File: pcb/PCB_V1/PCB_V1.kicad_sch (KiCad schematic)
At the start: 13 parts, among them U101 TPS54202DDCR

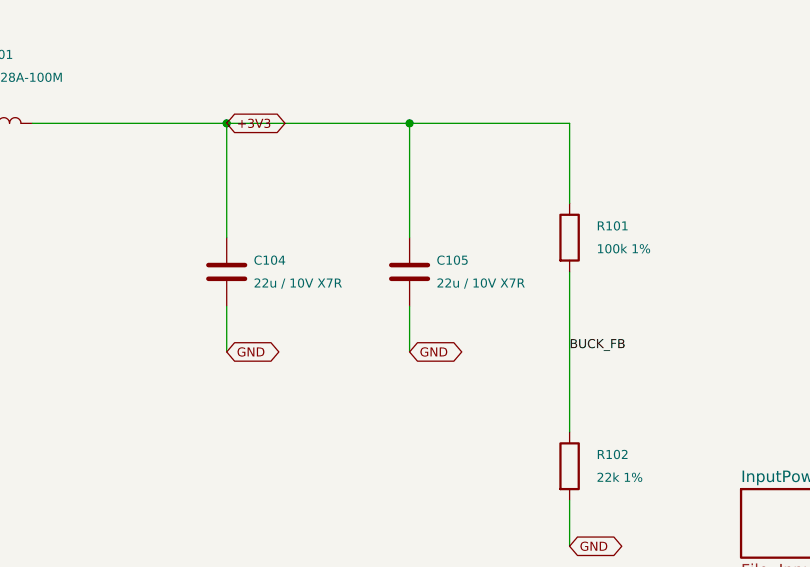
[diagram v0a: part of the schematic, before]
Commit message: pcb: revision 0.19 cost-down in the schematic, same footprints
Schematic and calculations only; PCB_V1.kicad_pcb is untouched on the
user's request. All substitutions keep footprints and nets.

- C716-C719, C726-C728: TDK C3225X7R2A106K250AC (X7R, published DC-bias
  curve 2.35 uF at 49 V) instead of Samsung CL32Y106KCV6PNE.
- C104/C105/C401: Samsung CL21A226MPQNNNE X5R; C521/C710/C715/C725/
  C905/C906: Taiyo Yuden UMK325AB7106KMHP.
- C602 shares CL21A106KAYNNNE with C201 (1.41 uF screen >= 1 uF);
  D601 shares SMBJ26CA with D901 (D_TVS symbol, 42.1 V clamp);
  R501/R511/R521 33R; F904 3 A shared with F721.
- analyze_led_power/analyze_power_path/verify_netlist updated; price and
  JLC snapshots v19; reports, sheet images and checks log v19.
- COST_DOWN.md: USD 37.50 per board (was 39.82), 65 purchase codes,
  rejected candidates and board status.

verify_board.py reports value differences for 17 parts until the board
is synced (footprints and nets already match); all other checks pass.

Co-Authored-By: Claude Opus 5.5 <noreply@anthropic.com>
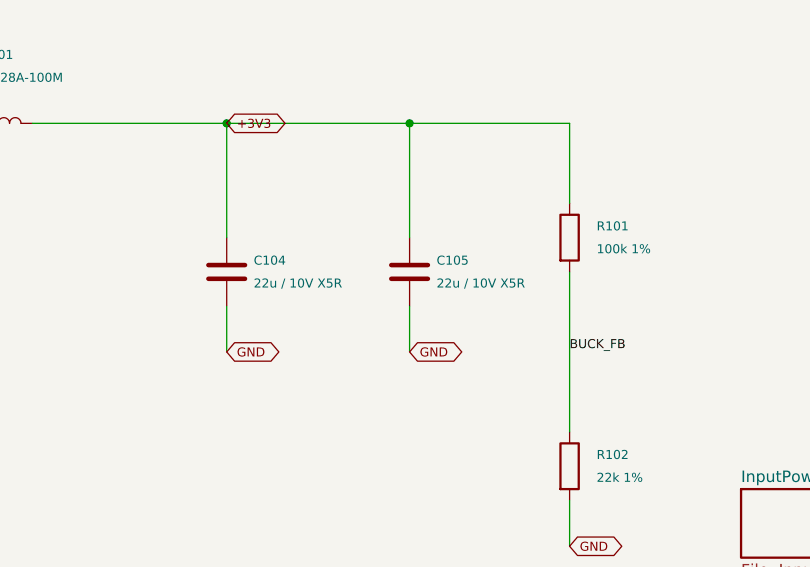
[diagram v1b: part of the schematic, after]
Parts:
- C104, C105: value 22u / 10V X7R -> 22u / 10V X5R; LCSC (none) -> C29277; MPN (none) -> CL21A226MPQNNNE; Manufacturer (none) -> Samsung Electro-Mechanics
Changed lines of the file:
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@@
 			)
 		)
-		(property "Value" "22u / 10V X7R"
+		(property "Value" "22u / 10V X5R"
 			(at 188.42 81.28 0)
 			(show_name no)
@@
 			)
 		)
-		(property "Datasheet" ""
+		(property "Datasheet" "https://product.samsungsem.com/mlcc/CL21A226MPQNNN.do"
 			(at 185.42 80.01 0)
 			(hide yes)
@@
 					(size 1.27 1.27)
 				)
+			)
+		)
+		(property "Manufacturer" "Samsung Electro-Mechanics"
+			(at 185.42 80.01 0)
+			(effects
+				(font
+					(size 1 1)
+				)
+				(hide yes)
+			)
+		)
+		(property "LCSC" "C29277"
+			(at 185.42 80.01 0)
+			(effects
+				(font
+					(size 1 1)
+				)
+				(hide yes)
+			)
+		)
+		(property "MPN" "CL21A226MPQNNNE"
+			(at 185.42 80.01 0)
+			(effects
+				(font
+					(size 1 1)
+				)
+				(hide yes)
 			)
 		)
@@
 			)
 		)
-		(property "Value" "22u / 10V X7R"
+		(property "Value" "22u / 10V X5R"
 			(at 168.1 81.28 0)
 			(show_name no)
@@
 			)
 		)
-		(property "Datasheet" ""
+		(property "Datasheet" "https://product.samsungsem.com/mlcc/CL21A226MPQNNN.do"
 			(at 165.1 80.01 0)
 			(hide yes)
@@
 			)
 		)
+		(property "Manufacturer" "Samsung Electro-Mechanics"
+			(at 165.1 80.01 0)
+			(effects
+				(font
+					(size 1 1)
+				)
+				(hide yes)
+			)
+		)
+		(property "LCSC" "C29277"
+			(at 165.1 80.01 0)
+			(effects
+				(font
+					(size 1 1)
+				)
+				(hide yes)
+			)
+		)
+		(property "MPN" "CL21A226MPQNNNE"
+			(at 165.1 80.01 0)
+			(effects
+				(font
+					(size 1 1)
+				)
+				(hide yes)
+			)
+		)

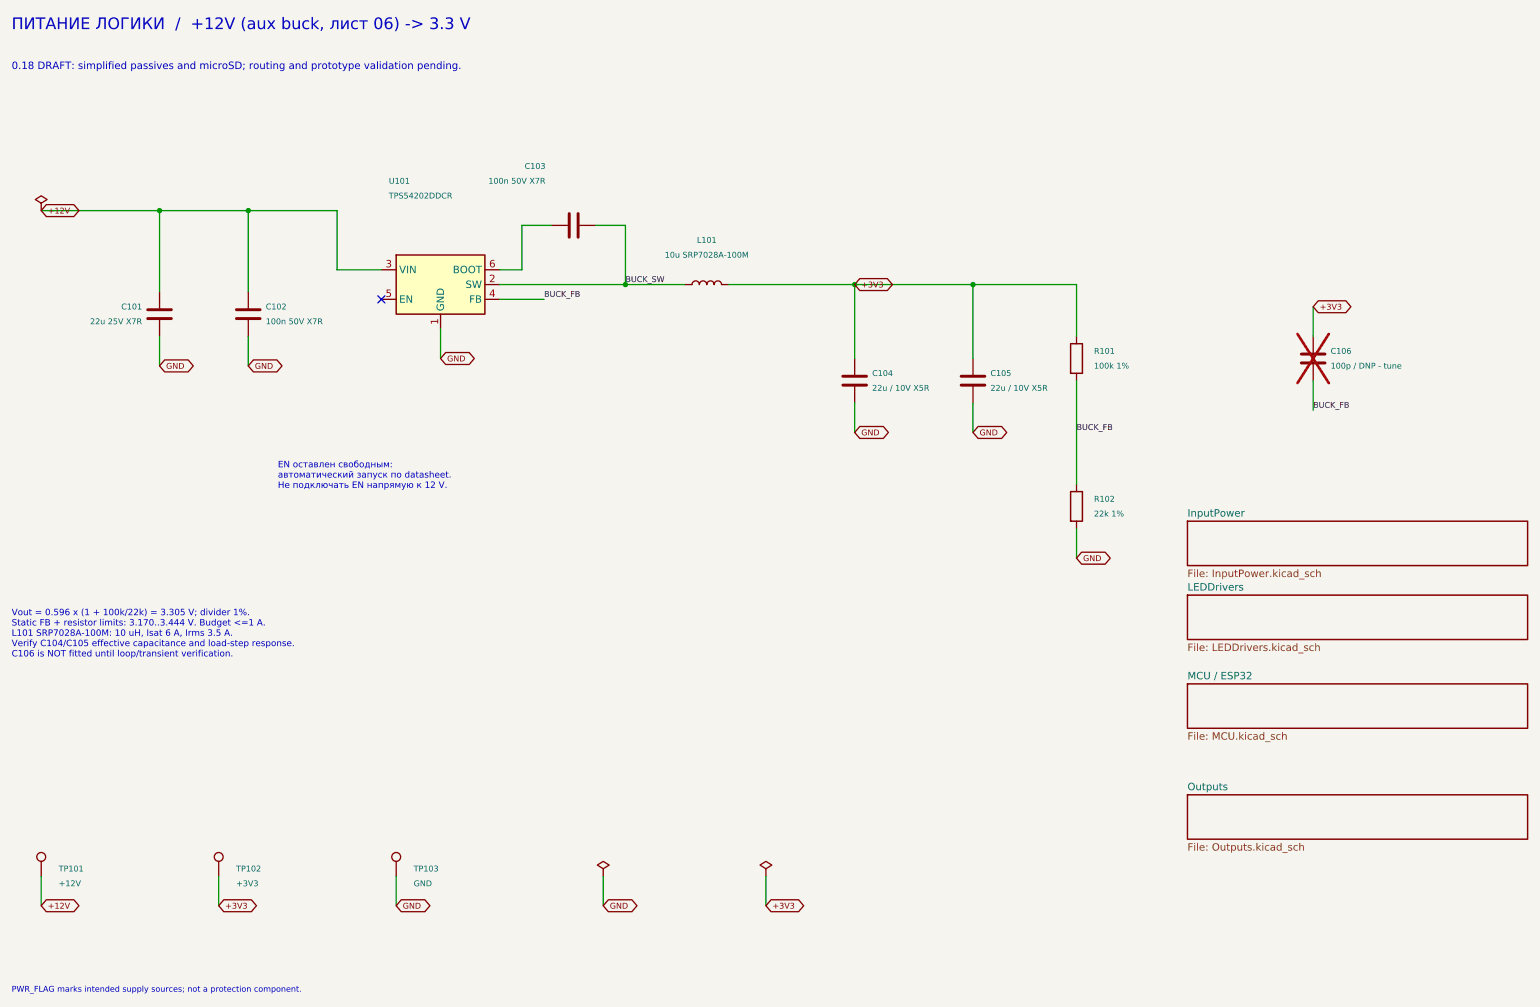
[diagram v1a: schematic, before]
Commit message: pcb: revision 0.20 cost-down with new footprints and placement
- RTC: DS3231MZ replaced by NXP PCF8563T/5 with an Epson FC-135 crystal
  (CL 12.5 pF), C304 18 pF C0G on OSCI, BAT54C supply OR (D303) and R307
  1k from the CR2032.
- Boost switches Q711/Q721: AOS AOD66923 (DPAK) on a project footprint
  that keeps the S1/2/3 G4 D5 numbering; diodes D711/D721: Vishay SS5P10
  (TO-277A).
- L101 cjiang FXL0630-100-M and L902 PROD PSPMAA0604-220M-ANP on the
  KiCad FXL0630 land.
- LED switch areas and the RTC cluster re-placed (29 parts moved);
  ERC 0, DRC 0, 340 unrouted links.
- Checks, price/JLC snapshots v20, reports, placement images and docs
  updated: USD 31.62 per board (29.52 for five boards).

Co-Authored-By: Claude Opus 5.5 <noreply@anthropic.com>
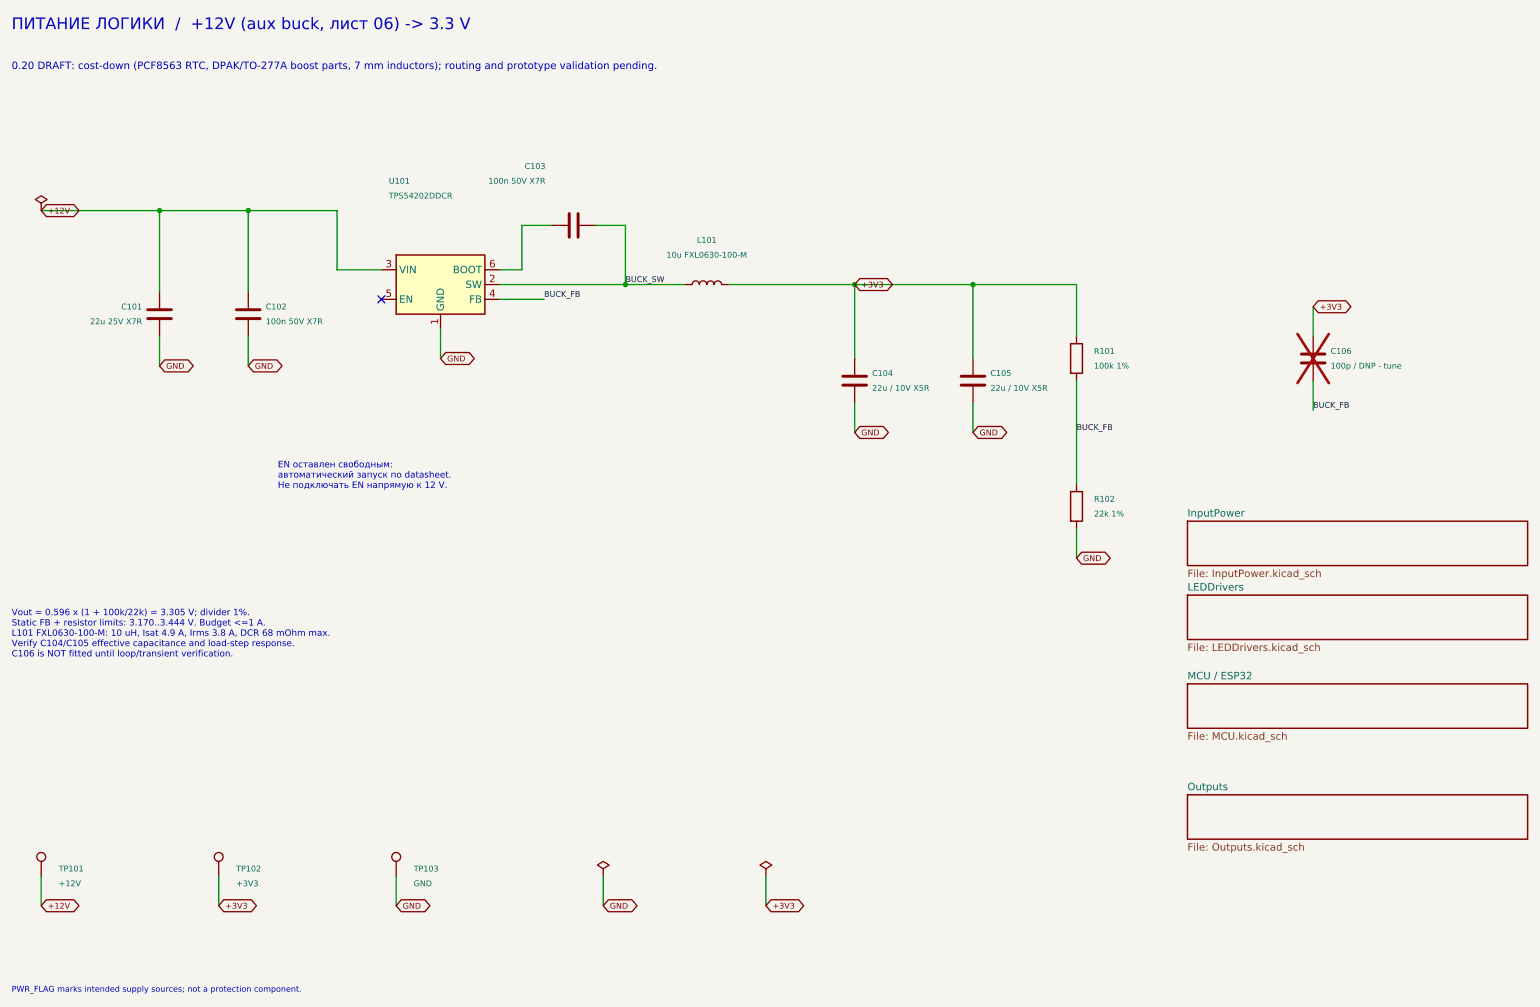
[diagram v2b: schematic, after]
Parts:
- L101: value 10u SRP7028A-100M -> 10u FXL0630-100-M; footprint Inductor_SMD:L_Bourns_SRP7028A_7.3x6.6mm -> Inductor_SMD:L_Changjiang_FXL0630; LCSC C2687402 -> C167223; MPN SRP7028A-100M -> FXL0630-100-M; Manufacturer Bourns -> cjiang
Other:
- note added: "0.20 DRAFT: cost-down (PCF8563 RTC, DPAK/TO-277A boost parts, 7 mm inductors); routing and prototype validation pending."
- note added: "Vout = 0.596 x (1 + 100k/22k) = 3.305 V; divider 1%. Static FB + resistor limits: 3.170..3.444 V. Budget <=1 A. L101 FXL0630-100-M: 10 uH, Isat 4.9 A, Irms 3.8 A, DCR 68 mOhm max. Verify C104/C105 effective capacitance and load-step response. C106 is NOT fitted until loop/transient verification."
- note removed: "0.18 DRAFT: simplified passives and microSD; routing and prototype validation pending."
- note removed: "Vout = 0.596 x (1 + 100k/22k) = 3.305 V; divider 1%. Static FB + resistor limits: 3.170..3.444 V. Budget <=1 A. L101 SRP7028A-100M: 10 uH, Isat 6 A, Irms 3.5 A. Verify C104/C105 effective capacitance and load-step response. C106 is NOT fitted until loop/transient verification."
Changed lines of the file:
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@@
 		(title "01 - Logic power / 12 V aux to 3.3 V")
 		(date "2026-09-29")
-		(rev "0.18-DRAFT")
+		(rev "0.20-DRAFT")
 		(company "GrowBox controller")
 		(comment 1 "Simplified prototype; unrouted; hardware qualification pending")
 	)
-	(text "Vout = 0.596 x (1 + 100k/22k) = 3.305 V; divider 1%.\nStatic FB + resistor limits: 3.170..3.444 V. Budget <=1 A.\nL101 SRP7028A-100M: 10 uH, Isat 6 A, Irms 3.5 A.\nVerify C104/C105 effective capacitance and load-step response.\nC106 is NOT fitted until loop/transient verification."
+	(text "Vout = 0.596 x (1 + 100k/22k) = 3.305 V; divider 1%.\nStatic FB + resistor limits: 3.170..3.444 V. Budget <=1 A.\nL101 FXL0630-100-M: 10 uH, Isat 4.9 A, Irms 3.8 A, DCR 68 mOhm max.\nVerify C104/C105 effective capacitance and load-step response.\nC106 is NOT fitted until loop/transient verification."
 		(exclude_from_sim no)
 		(at 20.32 119.38 0)
@@
 		)
 	)
-	(text "0.18 DRAFT: simplified passives and microSD; routing and prototype validation pending."
+	(text "0.20 DRAFT: cost-down (PCF8563 RTC, DPAK/TO-277A boost parts, 7 mm inductors); routing and prototype validation pending."
 		(exclude_from_sim no)
 		(at 20.32 25.4 0)
@@
 			)
 		)
-		(property "Value" "10u SRP7028A-100M"
+		(property "Value" "10u FXL0630-100-M"
 			(at 139.7 58.42 90)
 			(show_name no)
@@
 			)
 		)
-		(property "Footprint" "Inductor_SMD:L_Bourns_SRP7028A_7.3x6.6mm"
+		(property "Footprint" "Inductor_SMD:L_Changjiang_FXL0630"
 			(at 139.7 63.5 90)
 			(hide yes)
@@
 			)
 		)
-		(property "Datasheet" "https://www.bourns.com/docs/product-datasheets/srp7028a.pdf"
+		(property "Datasheet" "https://www.lcsc.com/product-detail/C167223.html"
 			(at 139.7 63.5 90)
 			(hide yes)
@@
 			)
 		)
-		(property "Manufacturer" "Bourns"
+		(property "Manufacturer" "cjiang"
 			(at 139.7 63.5 90)
 			(hide yes)
@@
 			)
 		)
-		(property "MPN" "SRP7028A-100M"
+		(property "MPN" "FXL0630-100-M"
 			(at 139.7 63.5 90)
 			(hide yes)
@@
 			)
 		)
-		(property "LCSC" "C2687402"
+		(property "LCSC" "C167223"
 			(at 139.7 63.5 90)
 			(hide yes)
